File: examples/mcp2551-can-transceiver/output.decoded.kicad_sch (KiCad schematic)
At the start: 5 parts, among them U1 MCP2551-I-SN

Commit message: Add footprint lookup table for TOKN decoder
- Add footprints.json with comprehensive lookup table:
  - Common passive sizes (0402, 0603, 0805, etc.)
  - IC packages (SOIC, TSSOP, QFN, LQFP, etc.)
  - Specific parts (MCP2551, MAX232, ATmega, STM32, etc.)
  - Transistors, regulators, op-amps, and more

- Update tokn_decoder.py to auto-populate footprints:
  - Priority: explicit > package hint > part match > passive type
  - Handles size codes (0603) for passives automatically

Decoded schematics now have proper footprints ready for PCB layout.
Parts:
- C60, C61: footprint (none) -> Capacitor_SMD:C_0603_1608Metric
- R1, R2: footprint (none) -> Resistor_SMD:R_0603_1608Metric
- U1: footprint SOIC-8 -> Package_SO:SOIC-8_3.9x4.9mm_P1.27mm
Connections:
- net +5V: now also U1.3; no longer U1.2
- net CAN0_HI: now also U1.7; no longer U1.6
- net CAN0_LO: now also U1.6; no longer U1.7
- net CAN0_RX: now also U1.4; no longer U1.5
- net CAN0_TX: now also U1.1; no longer U1.8
- net GND: now also U1.2; no longer U1.3
- net at R1.1: now also U1.8; no longer U1.1
- net at C60.1: now also U1.5; no longer U1.4
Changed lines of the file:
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@@
       (at 123.19 106.6 0)
       (effects (font (size 1.27 1.27))))
-    (property "Footprint" ""
+    (property "Footprint" "Capacitor_SMD:C_0603_1608Metric"
       (at 123.19 101.6 0)
       (effects (font (size 1.27 1.27)) (hide yes)))
@@
       (at 128.27 69.77 0)
       (effects (font (size 1.27 1.27))))
-    (property "Footprint" ""
+    (property "Footprint" "Capacitor_SMD:C_0603_1608Metric"
       (at 128.27 64.77 0)
       (effects (font (size 1.27 1.27)) (hide yes)))
@@
       (at 134.62 106.6 0)
       (effects (font (size 1.27 1.27))))
-    (property "Footprint" ""
+    (property "Footprint" "Resistor_SMD:R_0603_1608Metric"
       (at 134.62 101.6 0)
       (effects (font (size 1.27 1.27)) (hide yes)))
@@
       (at 172.72 90.09 0)
       (effects (font (size 1.27 1.27))))
-    (property "Footprint" ""
+    (property "Footprint" "Resistor_SMD:R_0603_1608Metric"
       (at 172.72 85.09 0)
       (effects (font (size 1.27 1.27)) (hide yes)))
@@
       (at 149.86 90.09 0)
       (effects (font (size 1.27 1.27))))
-    (property "Footprint" "SOIC-8"
+    (property "Footprint" "Package_SO:SOIC-8_3.9x4.9mm_P1.27mm"
       (at 149.86 85.09 0)
       (effects (font (size 1.27 1.27)) (hide yes)))

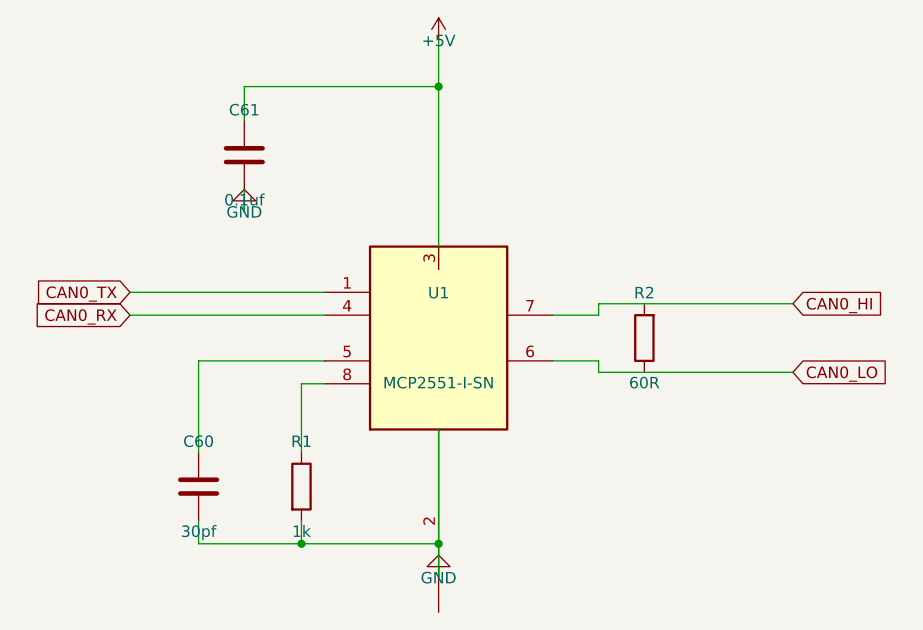
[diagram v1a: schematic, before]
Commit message: Fix decoder pin placement using TOKN pins section
- Use pin definitions from TOKN pins{REF}[N]: section instead of
  deriving positions from wire endpoints
- Calculate pin positions using standard dual-inline IC layout:
  pins 1-N/2 on left (top to bottom), N/2+1 to N on right (bottom to top)
- Include pin names from TOKN in generated lib_symbols
- Fix issue where pins with same net were merged to same position
- Regenerate all decoded schematics with correct pin placement
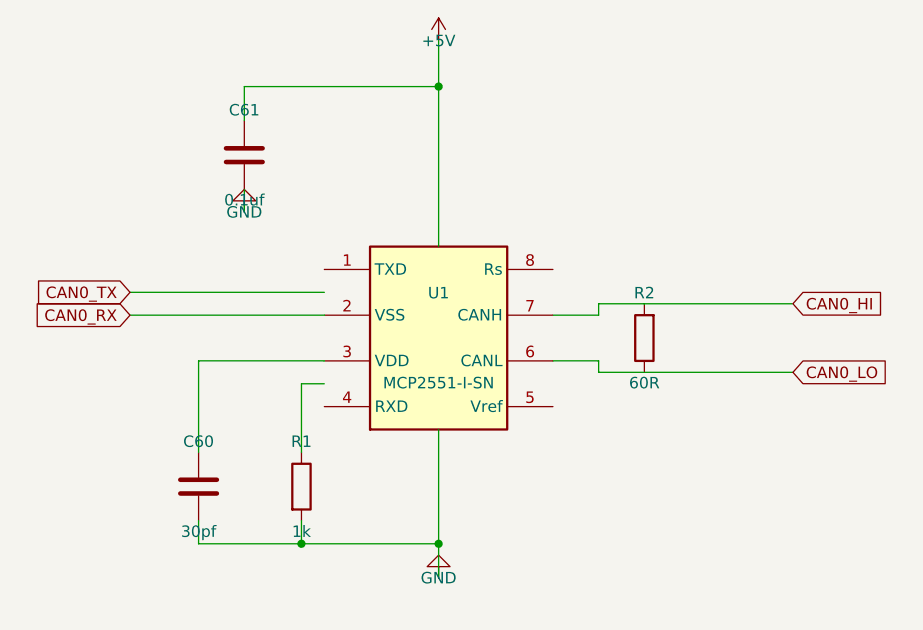
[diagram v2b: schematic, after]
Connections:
- net +5V: no longer U1.3
- net CAN0_RX: now also U1.2 (VSS); no longer U1.4
- net CAN0_TX: no longer U1.1
- net GND: no longer U1.2
- net at R1.1: no longer U1.8
- net at C60.1: now also U1.3 (VDD); no longer U1.5
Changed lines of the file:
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@@
       (at 149.86 85.09 0)
       (effects (font (size 1.27 1.27)) (hide yes)))
-    (pin "3"
+    (pin "1"
     )
     (pin "2"
     )
-    (pin "7"
+    (pin "3"
+    )
+    (pin "4"
+    )
+    (pin "5"
     )
     (pin "6"
     )
-    (pin "4"
-    )
-    (pin "1"
-    )
-    (pin "5"
+    (pin "7"
     )
     (pin "8"
